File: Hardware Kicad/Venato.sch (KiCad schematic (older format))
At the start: 24 parts, among them J1 Conn_01x02_Male, J2 Conn_01x02_Male, J3 Conn_01x02_Male, J4 Conn_01x02_Male, J5 Conn_01x02_Male, J6 Conn_01x02_Male, J7 Conn_01x05_Male, U1 LM317_TO-220, U2 MCP6002-xP, U3 MCP6002-xP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

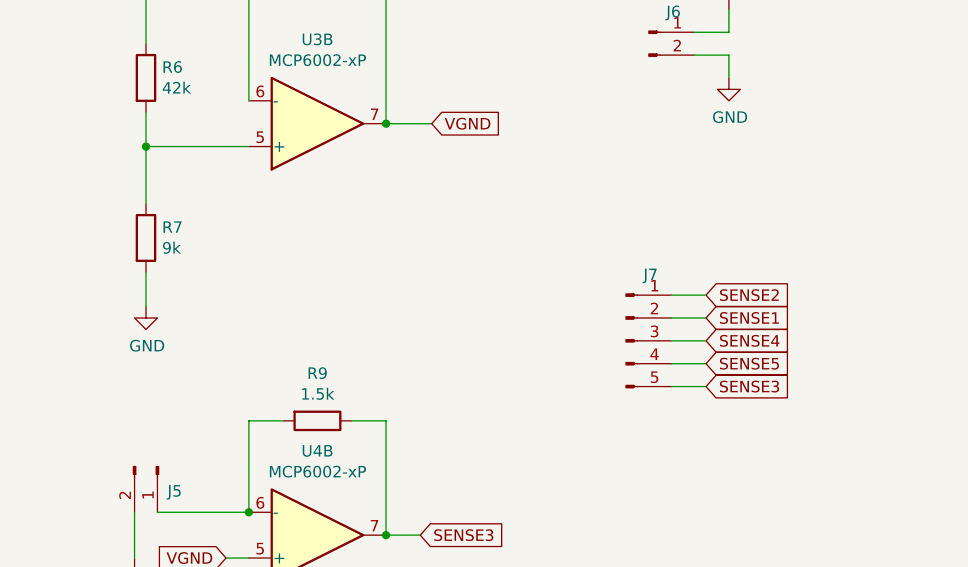
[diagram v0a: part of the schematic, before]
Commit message: 1mm traces and fix resistor
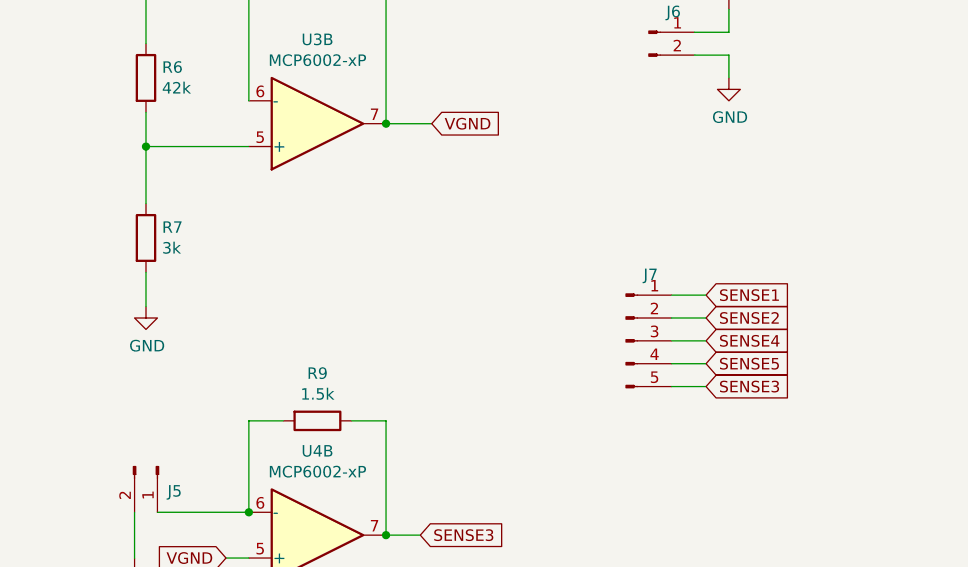
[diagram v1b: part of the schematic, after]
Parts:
- R7: value 9k -> 3k
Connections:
- net SENSE1: now also J7.1 (Pin_1); no longer J7.2 (Pin_2)
- net SENSE2: now also J7.2 (Pin_2); no longer J7.1 (Pin_1)
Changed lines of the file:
@@
 P 3450 4200
 F 0 "R7" H 3520 4246 50  0000 L CNN
-F 1 "9k" H 3520 4155 50  0000 L CNN
+F 1 "3k" H 3520 4155 50  0000 L CNN
 F 2 "Resistor_THT:R_Axial_DIN0204_L3.6mm_D1.6mm_P7.62mm_Horizontal" V 3380 4200 50  0001 C CNN
 F 3 "~" H 3450 4200 50  0001 C CNN
@@
 	1    0    0    -1
 $EndComp
-Text GLabel 5900 4550 2    50   Input ~ 0
+Text GLabel 5900 4450 2    50   Input ~ 0
 SENSE1
 Text GLabel 5900 4650 2    50   Input ~ 0
@@
 Text GLabel 5900 4850 2    50   Input ~ 0
 SENSE3
-Text GLabel 5900 4450 2    50   Input ~ 0
+Text GLabel 5900 4550 2    50   Input ~ 0
 SENSE2
 $EndSCHEMATC
